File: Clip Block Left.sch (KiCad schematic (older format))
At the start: 18 parts, among them J15 Conn_01x08_Female, SW1 SW_SPST_4_PIN, SW10 SW_SPST_4_PIN, SW11 SW_SPST_4_PIN, SW12 SW_SPST_4_PIN, SW13 SW_SPST_4_PIN, SW14 SW_SPST_4_PIN, SW15 SW_SPST_4_PIN, SW16 SW_SPST_4_PIN, SW2 SW_SPST_4_PIN, SW3 SW_SPST_4_PIN, SW4 SW_SPST_4_PIN, SW5 SW_SPST_4_PIN, SW6 SW_SPST_4_PIN, SW7 SW_SPST_4_PIN, SW8 SW_SPST_4_PIN, SW9 SW_SPST_4_PIN, U1 CD74HC4067M

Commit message: Beginning button connections
Beginning running traces to the button blocks modified schematic to ensure minimum trace length, rotate buttons to achieve this.
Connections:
- wire segments 114 -> 116
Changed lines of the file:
@@
 	3750 1800 5050 1800
 Wire Wire Line
-	5350 1650 5350 2550
-Wire Wire Line
-	5450 1600 5450 2050
-Wire Wire Line
-	5450 2050 5600 2050
-Wire Wire Line
-	2900 1550 5600 1550
-Wire Wire Line
-	5350 2550 5600 2550
+	2900 1550 5550 1550
 Wire Wire Line
 	3350 1600 5450 1600
@@
 Wire Wire Line
 	2400 3450 2400 3350
-NoConn ~ 5600 1650
 NoConn ~ 6000 1650
 NoConn ~ 4500 2450
@@
 NoConn ~ 4100 4950
 NoConn ~ 4100 4450
-NoConn ~ 5600 2150
 NoConn ~ 6000 2150
 NoConn ~ 6000 2650
-NoConn ~ 5600 2650
 NoConn ~ 6000 3150
 NoConn ~ 6000 3650
@@
 	3750 2650 3750 3950
 Wire Wire Line
-	5250 1700 5250 3050
-Wire Wire Line
-	5150 3650 5600 3650
-Wire Wire Line
-	5150 1750 5150 3650
-Wire Wire Line
-	5050 4150 5600 4150
-Wire Wire Line
-	5050 1800 5050 4150
-Wire Wire Line
-	4950 4650 5600 4650
-Wire Wire Line
-	4950 1850 4950 4650
-NoConn ~ 5600 3550
-NoConn ~ 5600 4050
-NoConn ~ 5600 4550
-Wire Wire Line
-	5250 3050 5600 3050
-NoConn ~ 5600 3150
+	5150 1750 5150 3550
+Wire Wire Line
+	5050 1800 5050 4050
+Wire Wire Line
+	4950 1850 4950 4550
 NoConn ~ 4100 2350
 NoConn ~ 4100 2850
 NoConn ~ 4100 3350
 NoConn ~ 4100 3850
-NoConn ~ 5600 5050
-Wire Wire Line
-	4850 5150 5600 5150
-Wire Wire Line
-	4850 1900 4850 5150
+Wire Wire Line
+	4850 1900 4850 5050
+Wire Wire Line
+	5600 5050 4850 5050
+Wire Wire Line
+	5600 4550 4950 4550
+NoConn ~ 5600 5150
+NoConn ~ 5600 4650
+Wire Wire Line
+	5600 3550 5150 3550
+Wire Wire Line
+	5050 4050 5600 4050
+NoConn ~ 5600 4150
+NoConn ~ 5600 3650
+Wire Wire Line
+	5600 3150 5250 3150
+Wire Wire Line
+	5600 2650 5350 2650
+Wire Wire Line
+	5600 2150 5450 2150
+Wire Wire Line
+	5600 1650 5550 1650
+Wire Wire Line
+	5550 1650 5550 1550
+Wire Wire Line
+	5450 1600 5450 2150
+Wire Wire Line
+	5350 1650 5350 2650
+Wire Wire Line
+	5250 1700 5250 3150
+NoConn ~ 5600 3050
+NoConn ~ 5600 2550
+NoConn ~ 5600 2050
+NoConn ~ 5600 1550
 $EndSCHEMATC

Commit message: Further work on the separate boards
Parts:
- SW1, SW10, SW11, SW12, SW13, SW14, SW15, SW16, SW2, SW3, SW4, SW5, SW6, SW7, SW8, SW9: symbol sw_spst_0:SW_SPST_4_PIN -> cp_midi_control_surface_002-rescue:SW_SPST_4_PIN-sw_spst_0
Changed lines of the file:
@@
 $EndDescr
 $Comp
-L sw_spst_0:SW_SPST_4_PIN SW1
+L cp_midi_control_surface_002-rescue:SW_SPST_4_PIN-sw_spst_0 SW1
 U 1 1 5C4BAAC6
 P 5800 1550
+AR Path="/5C4BAAC6" Ref="SW1"  Part="1"
+AR Path="/5C4B73B3/5C4BAAC6" Ref="SW1"  Part="1"
 F 0 "SW1" H 5800 1300 50  0000 C CNN
 F 1 "SW_SPST_4_PIN" H 5800 1724 50  0001 C CNN
@@
 $EndComp
 $Comp
-L sw_spst_0:SW_SPST_4_PIN SW2
+L cp_midi_control_surface_002-rescue:SW_SPST_4_PIN-sw_spst_0 SW2
 U 1 1 5C4BAAC7
 P 5800 2050
+AR Path="/5C4BAAC7" Ref="SW2"  Part="1"
+AR Path="/5C4B73B3/5C4BAAC7" Ref="SW2"  Part="1"
 F 0 "SW2" H 5800 1850 50  0000 C CNN
 F 1 "SW_SPST_4_PIN" H 5800 2224 50  0001 C CNN
@@
 $EndComp
 $Comp
-L sw_spst_0:SW_SPST_4_PIN SW3
+L cp_midi_control_surface_002-rescue:SW_SPST_4_PIN-sw_spst_0 SW3
 U 1 1 5C4BAAC8
 P 5800 2550
+AR Path="/5C4BAAC8" Ref="SW3"  Part="1"
+AR Path="/5C4B73B3/5C4BAAC8" Ref="SW3"  Part="1"
 F 0 "SW3" H 5800 2350 50  0000 C CNN
 F 1 "SW_SPST_4_PIN" H 5800 2724 50  0001 C CNN
@@
 $EndComp
 $Comp
-L sw_spst_0:SW_SPST_4_PIN SW4
+L cp_midi_control_surface_002-rescue:SW_SPST_4_PIN-sw_spst_0 SW4
 U 1 1 5C4BAAC9
 P 5800 3050
+AR Path="/5C4BAAC9" Ref="SW4"  Part="1"
+AR Path="/5C4B73B3/5C4BAAC9" Ref="SW4"  Part="1"
 F 0 "SW4" H 5800 2850 50  0000 C CNN
 F 1 "SW_SPST_4_PIN" H 5800 3224 50  0001 C CNN
@@
 $EndComp
 $Comp
-L sw_spst_0:SW_SPST_4_PIN SW5
+L cp_midi_control_surface_002-rescue:SW_SPST_4_PIN-sw_spst_0 SW5
 U 1 1 5C4B764F
 P 5800 3550
+AR Path="/5C4B764F" Ref="SW5"  Part="1"
+AR Path="/5C4B73B3/5C4B764F" Ref="SW5"  Part="1"
 F 0 "SW5" H 5800 3350 50  0000 C CNN
 F 1 "SW_SPST_4_PIN" H 5800 3724 50  0001 C CNN
@@
 $EndComp
 $Comp
-L sw_spst_0:SW_SPST_4_PIN SW6
+L cp_midi_control_surface_002-rescue:SW_SPST_4_PIN-sw_spst_0 SW6
 U 1 1 5C4B8146
 P 5800 4050
+AR Path="/5C4B8146" Ref="SW6"  Part="1"
+AR Path="/5C4B73B3/5C4B8146" Ref="SW6"  Part="1"
 F 0 "SW6" H 5800 3850 50  0000 C CNN
 F 1 "SW_SPST_4_PIN" H 5800 4224 50  0001 C CNN
@@
 $EndComp
 $Comp
-L sw_spst_0:SW_SPST_4_PIN SW7
+L cp_midi_control_surface_002-rescue:SW_SPST_4_PIN-sw_spst_0 SW7
 U 1 1 5C4B814C
 P 5800 4550
+AR Path="/5C4B814C" Ref="SW7"  Part="1"
+AR Path="/5C4B73B3/5C4B814C" Ref="SW7"  Part="1"
 F 0 "SW7" H 5800 4350 50  0000 C CNN
 F 1 "SW_SPST_4_PIN" H 5800 4724 50  0001 C CNN
@@
 $EndComp
 $Comp
-L sw_spst_0:SW_SPST_4_PIN SW8
+L cp_midi_control_surface_002-rescue:SW_SPST_4_PIN-sw_spst_0 SW8
 U 1 1 5C4B8152
 P 5800 5050
+AR Path="/5C4B8152" Ref="SW8"  Part="1"
+AR Path="/5C4B73B3/5C4B8152" Ref="SW8"  Part="1"
 F 0 "SW8" H 5800 4850 50  0000 C CNN
 F 1 "SW_SPST_4_PIN" H 5800 5224 50  0001 C CNN
@@
 $EndComp
 $Comp
-L sw_spst_0:SW_SPST_4_PIN SW9
+L cp_midi_control_surface_002-rescue:SW_SPST_4_PIN-sw_spst_0 SW9
 U 1 1 5C4B907B
 P 4300 2350
+AR Path="/5C4B907B" Ref="SW9"  Part="1"
+AR Path="/5C4B73B3/5C4B907B" Ref="SW9"  Part="1"
 F 0 "SW9" H 4300 2150 50  0000 C CNN
 F 1 "SW_SPST_4_PIN" H 5000 2300 50  0001 C CNN
@@
 $EndComp
 $Comp
-L sw_spst_0:SW_SPST_4_PIN SW10
+L cp_midi_control_surface_002-rescue:SW_SPST_4_PIN-sw_spst_0 SW10
 U 1 1 5C4B9081
 P 4300 2850
+AR Path="/5C4B9081" Ref="SW10"  Part="1"
+AR Path="/5C4B73B3/5C4B9081" Ref="SW10"  Part="1"
 F 0 "SW10" H 4300 2650 50  0000 C CNN
 F 1 "SW_SPST_4_PIN" H 4300 3024 50  0001 C CNN
@@
 $EndComp
 $Comp
-L sw_spst_0:SW_SPST_4_PIN SW11
+L cp_midi_control_surface_002-rescue:SW_SPST_4_PIN-sw_spst_0 SW11
 U 1 1 5C4B9087
 P 4300 3350
+AR Path="/5C4B9087" Ref="SW11"  Part="1"
+AR Path="/5C4B73B3/5C4B9087" Ref="SW11"  Part="1"
 F 0 "SW11" H 4300 3150 50  0000 C CNN
 F 1 "SW_SPST_4_PIN" H 4300 3524 50  0001 C CNN
@@
 $EndComp
 $Comp
-L sw_spst_0:SW_SPST_4_PIN SW12
+L cp_midi_control_surface_002-rescue:SW_SPST_4_PIN-sw_spst_0 SW12
 U 1 1 5C4B908D
 P 4300 3850
+AR Path="/5C4B908D" Ref="SW12"  Part="1"
+AR Path="/5C4B73B3/5C4B908D" Ref="SW12"  Part="1"
 F 0 "SW12" H 4300 3650 50  0000 C CNN
 F 1 "SW_SPST_4_PIN" H 4300 4024 50  0001 C CNN
@@
 $EndComp
 $Comp
-L sw_spst_0:SW_SPST_4_PIN SW13
+L cp_midi_control_surface_002-rescue:SW_SPST_4_PIN-sw_spst_0 SW13
 U 1 1 5C4B9093
 P 4300 4350
+AR Path="/5C4B9093" Ref="SW13"  Part="1"
+AR Path="/5C4B73B3/5C4B9093" Ref="SW13"  Part="1"
 F 0 "SW13" H 4300 4150 50  0000 C CNN
 F 1 "SW_SPST_4_PIN" H 4300 4524 50  0001 C CNN
@@
 $EndComp
 $Comp
-L sw_spst_0:SW_SPST_4_PIN SW14
+L cp_midi_control_surface_002-rescue:SW_SPST_4_PIN-sw_spst_0 SW14
 U 1 1 5C4B9099
 P 4300 4850
+AR Path="/5C4B9099" Ref="SW14"  Part="1"
+AR Path="/5C4B73B3/5C4B9099" Ref="SW14"  Part="1"
 F 0 "SW14" H 4300 4650 50  0000 C CNN
 F 1 "SW_SPST_4_PIN" H 4300 5024 50  0001 C CNN
@@
 $EndComp
 $Comp
-L sw_spst_0:SW_SPST_4_PIN SW15
+L cp_midi_control_surface_002-rescue:SW_SPST_4_PIN-sw_spst_0 SW15
 U 1 1 5C4B909F
 P 4300 5350
+AR Path="/5C4B909F" Ref="SW15"  Part="1"
+AR Path="/5C4B73B3/5C4B909F" Ref="SW15"  Part="1"
 F 0 "SW15" H 4300 5150 50  0000 C CNN
 F 1 "SW_SPST_4_PIN" H 4300 5524 50  0001 C CNN
@@
 $EndComp
 $Comp
-L sw_spst_0:SW_SPST_4_PIN SW16
+L cp_midi_control_surface_002-rescue:SW_SPST_4_PIN-sw_spst_0 SW16
 U 1 1 5C4B90A5
 P 4300 5850
+AR Path="/5C4B90A5" Ref="SW16"  Part="1"
+AR Path="/5C4B73B3/5C4B90A5" Ref="SW16"  Part="1"
 F 0 "SW16" H 4300 5650 50  0000 C CNN
 F 1 "SW_SPST_4_PIN" H 4300 6024 50  0001 C CNN

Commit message: Sub boards completed
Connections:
- net GND: now also SW1.4; no longer SW1.3
- net at U1.13 (S3): now also J15.3 (Pin_3); no longer J15.4 (Pin_4)
- net at U1.14 (S2): now also J15.4 (Pin_4); no longer J15.3 (Pin_3)
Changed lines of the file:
@@
 	3650 1950 3650 1750
-Wire Wire Line
-	6000 1550 6150 1550
-Wire Wire Line
-	6150 1550 6150 2050
 Wire Wire Line
 	6150 5850 4650 5850
@@
 Wire Wire Line
 	2400 3450 2400 3350
-NoConn ~ 6000 1650
 NoConn ~ 4500 2450
 NoConn ~ 4500 2950
@@
 NoConn ~ 950  2850
 Wire Wire Line
-	950  2450 1900 2450
-Wire Wire Line
 	950  2150 1900 2150
 Wire Wire Line
 	950  2250 1900 2250
-Wire Wire Line
-	950  2350 1900 2350
 Wire Wire Line
 	1600 2550 1600 1750
@@
 NoConn ~ 5600 2050
 NoConn ~ 5600 1550
+Wire Wire Line
+	1400 2450 1400 2350
+Wire Wire Line
+	1400 2350 950  2350
+Wire Wire Line
+	1900 2450 1400 2450
+Wire Wire Line
+	1900 2350 1700 2350
+Wire Wire Line
+	1700 2350 1700 2400
+Wire Wire Line
+	1700 2400 1200 2400
+Wire Wire Line
+	1200 2400 1200 2450
+Wire Wire Line
+	1200 2450 950  2450
+NoConn ~ 6000 1550
+Wire Wire Line
+	6000 1650 6150 1650
+Wire Wire Line
+	6150 1650 6150 2050
 $EndSCHEMATC

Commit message: Tidy schematic / renumber components / complete daughter boards
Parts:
- J1: renamed from J15; value Conn_01x08_Female -> ~; symbol Connector:Conn_01x08_Female -> Connector:Conn_01x08_Male
- SW1, SW10, SW11, SW12, SW13, SW14, SW15, SW16, SW2, SW3, SW4, SW5, SW6, SW7, SW8, SW9: value SW_SPST_4_PIN -> B3F-5050
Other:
- moved on the sheet: SW1, SW10, SW11, SW12, SW13, SW14, SW15, SW16, SW2, SW3, SW4, SW5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

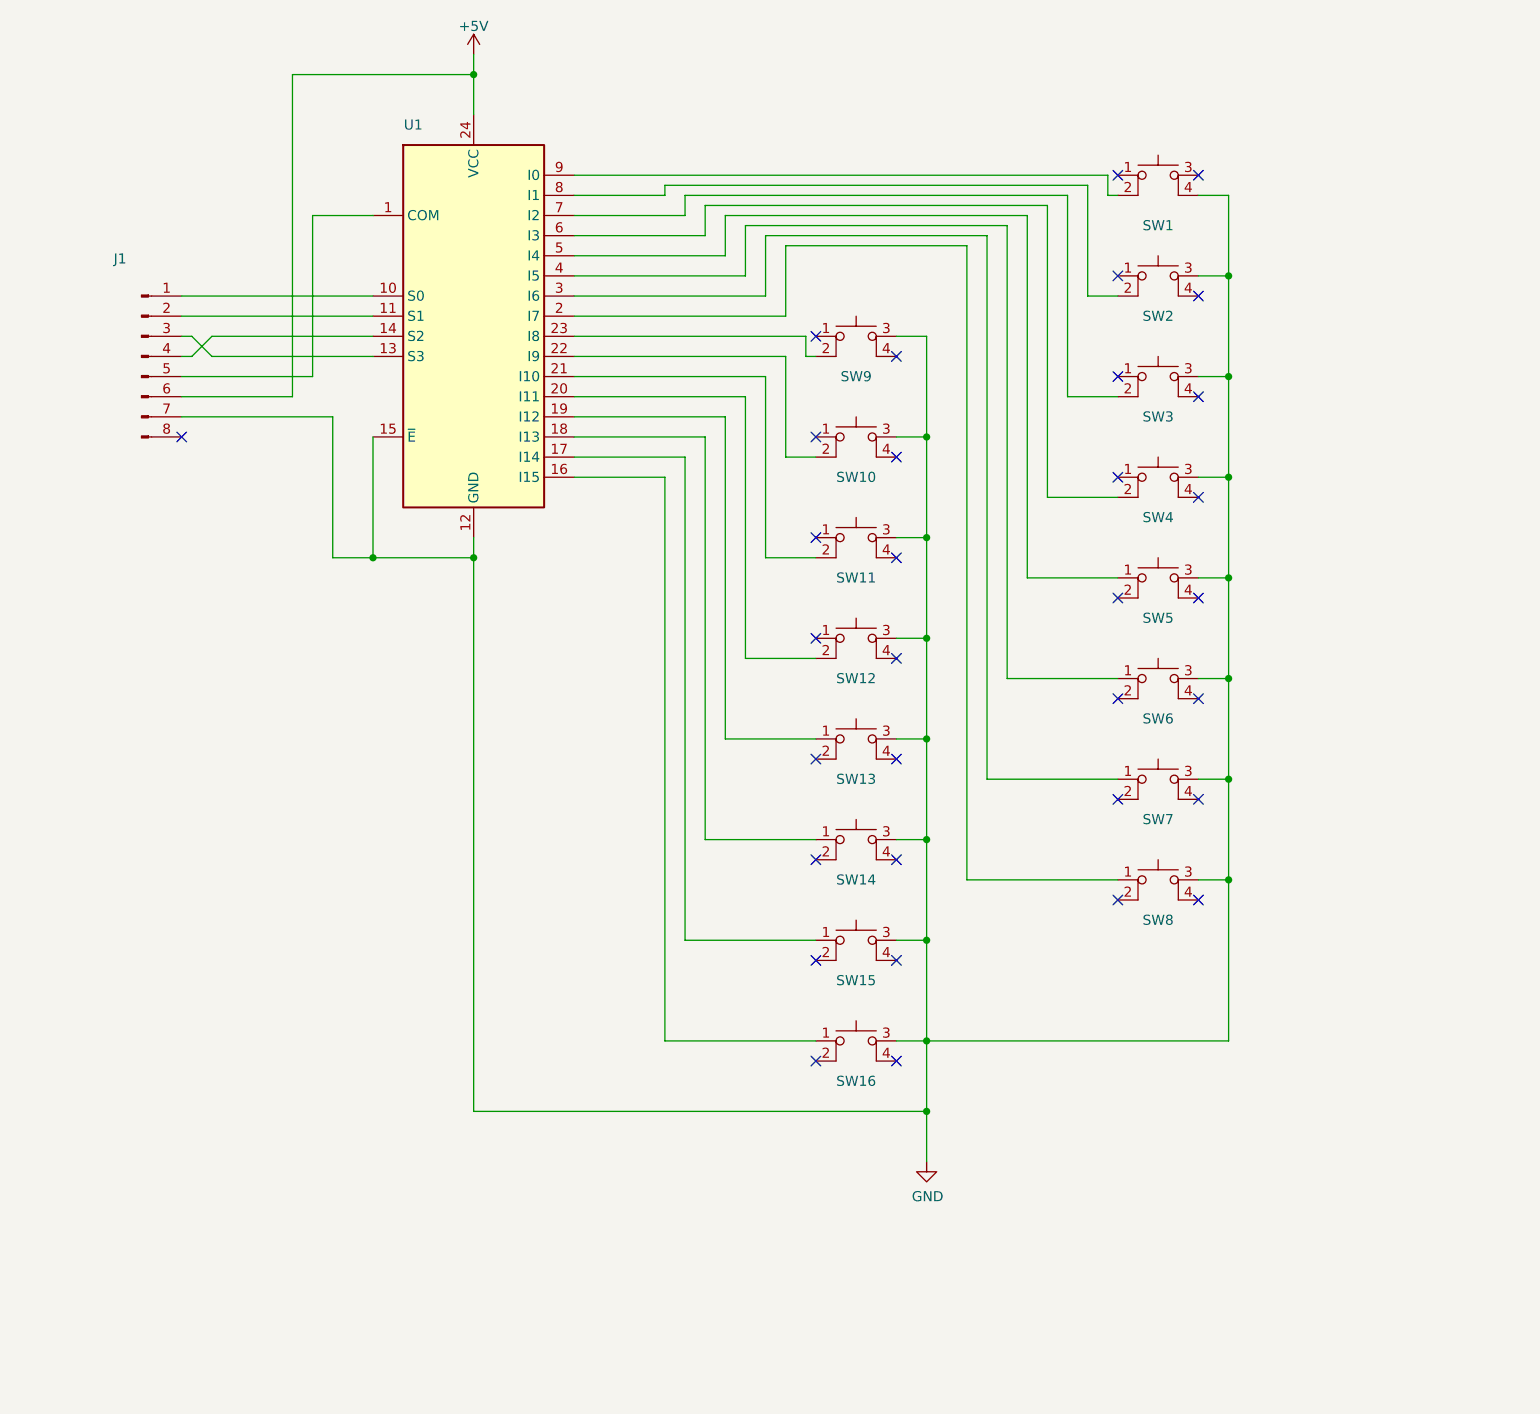
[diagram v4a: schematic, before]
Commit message: Redesign of upper boards
Added bussed resistors following Igor's correction to the schematic + tidied schematic.
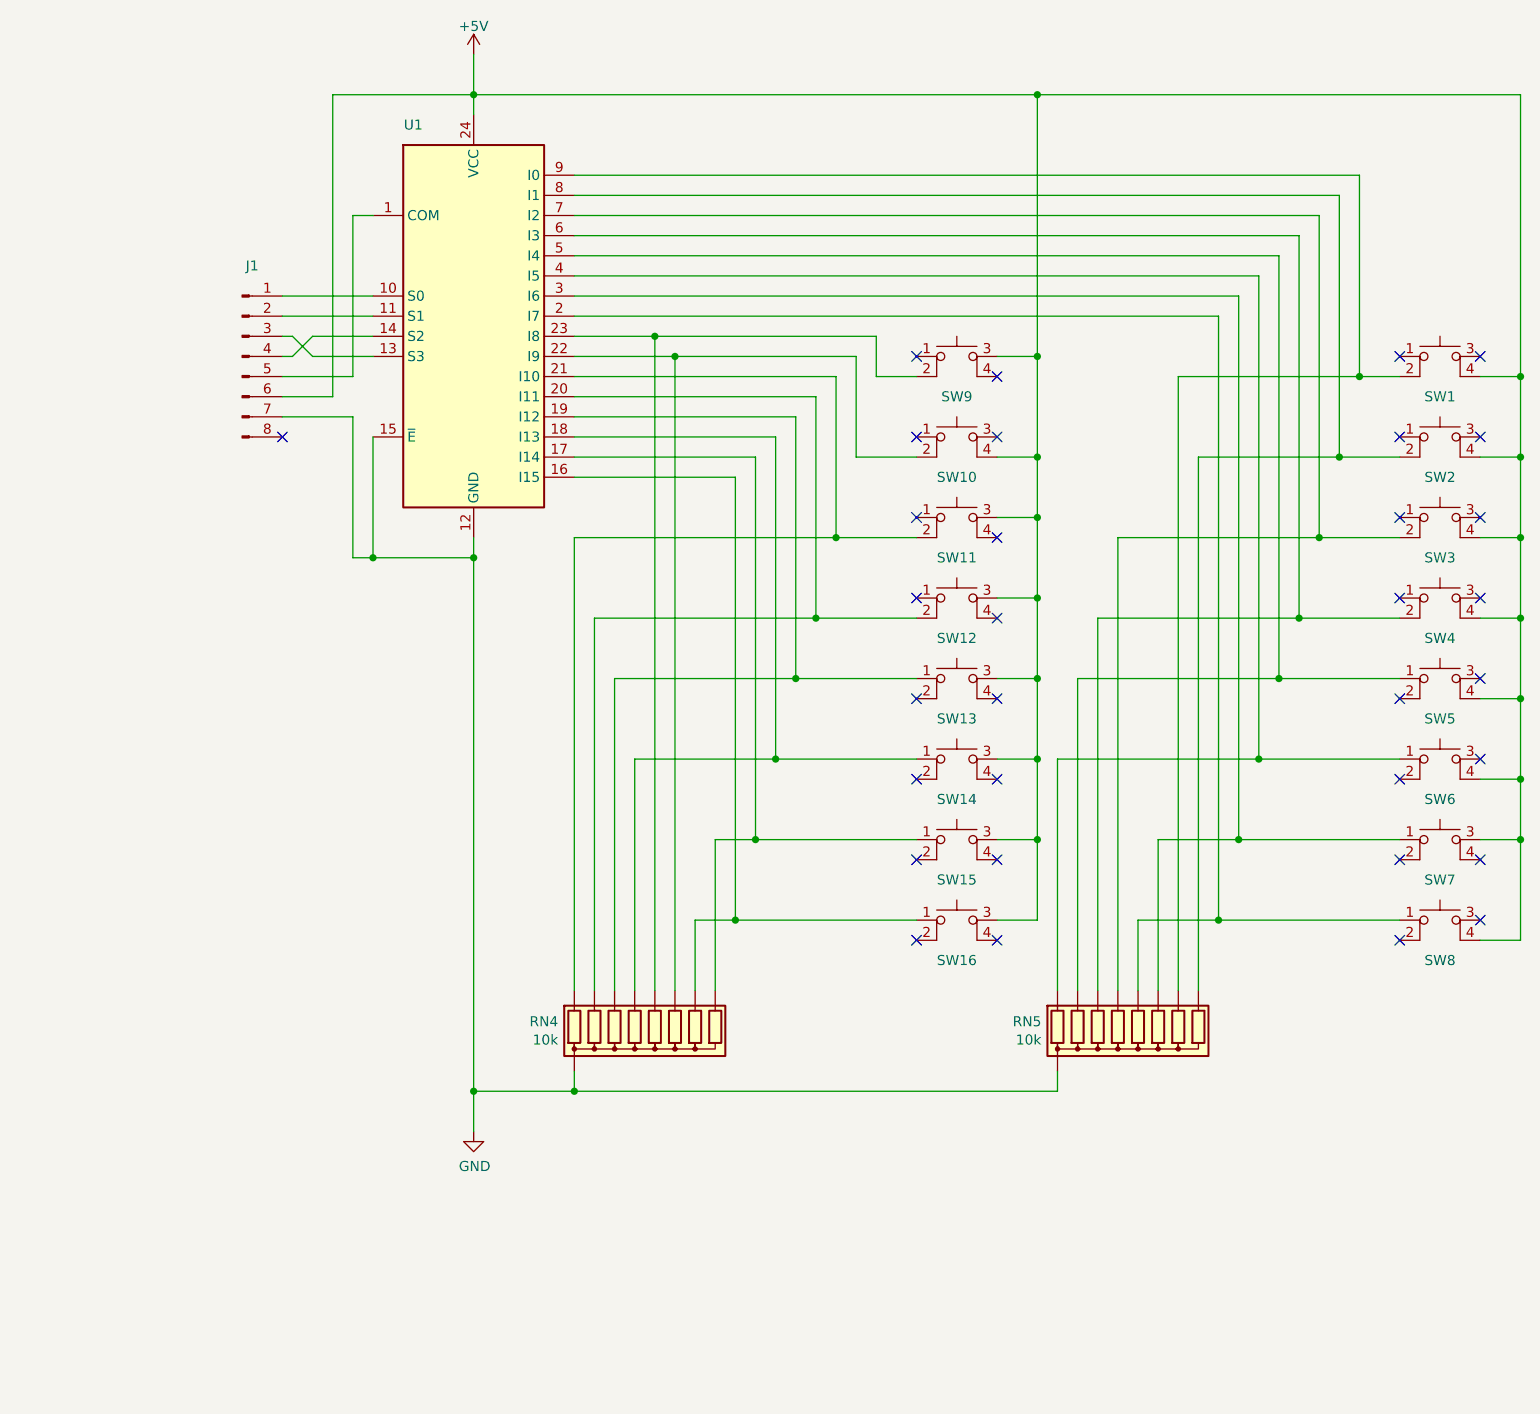
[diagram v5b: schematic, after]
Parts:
- added RN4, RN5: 10k, Resistor_THT:R_Array_SIP9, symbol Device:R_Network08
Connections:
- net +5V: now also SW1.4, SW10.4, SW11.3, SW12.3, SW13.3, SW14.3, SW15.3, SW16.3, SW2.4, SW3.4, SW4.4, SW5.4, SW6.4, SW7.3, SW8.4, SW9.3
- net GND: now also RN4.1 (common), RN5.1 (common); no longer SW1.4, SW10.3, SW11.3, SW12.3, SW13.3, SW14.3, SW15.3, SW16.3, SW2.3, SW3.3, SW4.3, SW5.3, SW6.3, SW7.3, SW8.3, SW9.3
- net at SW5.1 (A), U1.5 (I4): now also RN5.3 (R2)
- net at SW6.1 (A), U1.4 (I5): now also RN5.2 (R1)
- net at SW7.1 (A), U1.3 (I6): now also RN5.7 (R6)
- net at SW8.1 (A), U1.2 (I7): now also RN5.6 (R5)
- net at SW9.2, U1.23 (I8): now also RN4.6 (R5)
- net at SW10.2, U1.22 (I9): now also RN4.7 (R6)
- net at SW11.2, U1.21 (I10): now also RN4.2 (R1)
- net at SW12.2, U1.20 (I11): now also RN4.3 (R2)
- net at SW13.1 (A), U1.19 (I12): now also RN4.4 (R3)
- net at SW14.1 (A), U1.18 (I13): now also RN4.5 (R4)
- net at SW15.1 (A), U1.17 (I14): now also RN4.9 (R8)
- net at SW16.1 (A), U1.16 (I15): now also RN4.8 (R7)
- net at SW1.2, U1.9 (I0): now also RN5.8 (R7)
- net at SW2.2, U1.8 (I1): now also RN5.9 (R8)
- net at SW3.2, U1.7 (I2): now also RN5.5 (R4)
- net at SW4.2, U1.6 (I3): now also RN5.4 (R3)
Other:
- moved on the sheet: J1, SW1, SW10, SW11, SW12, SW13, SW14, SW15, SW16, SW2, SW3, SW4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
